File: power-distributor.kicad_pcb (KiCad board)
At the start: 2 copper layers, 99.8 x 18.7 mm, 9 parts, among them J11 Barrel_Jack, J21 Barrel_Jack, J22 Barrel_Jack, J23 Barrel_Jack, J24 Barrel_Jack, J25 Barrel_Jack

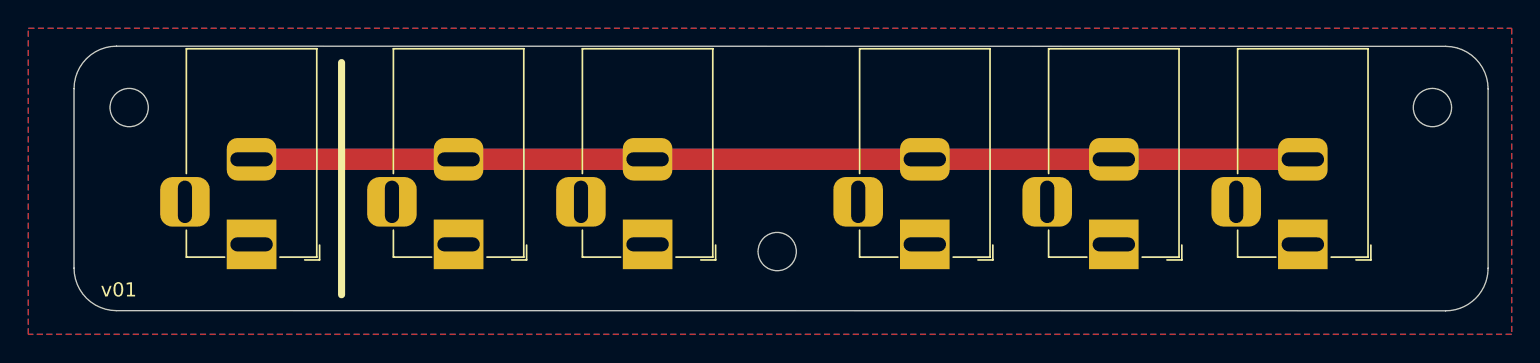
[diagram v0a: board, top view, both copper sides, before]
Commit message: v02: Bigger mounting holes, more even spacing
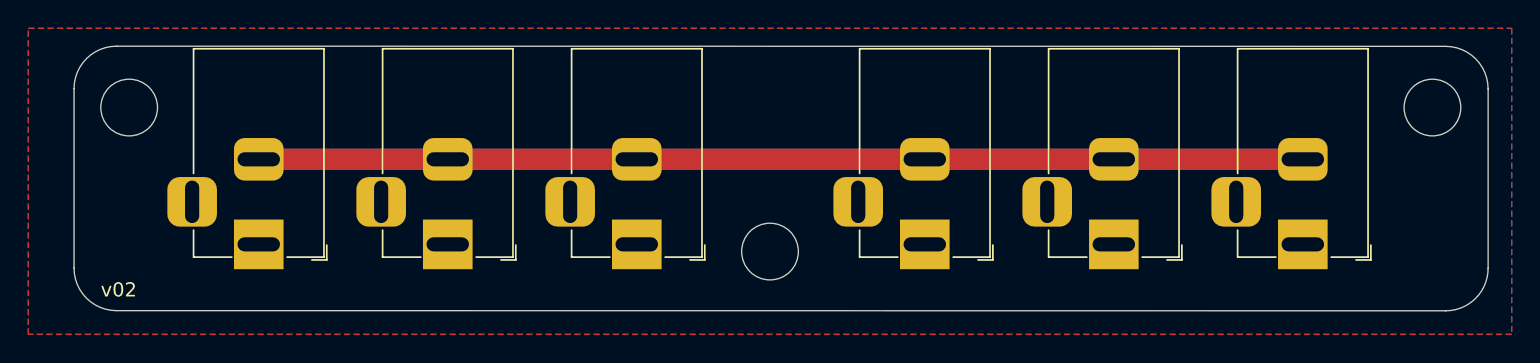
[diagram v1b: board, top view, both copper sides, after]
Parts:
- moved J2 0.76 mm to (92.6, 96.5)
- moved J3 0.76 mm to (105.9, 96.5)
- moved J1 0.51 mm to (79.2, 96.5)
- moved H2 0.51 mm to (115.3, 97.0)
- renumbered J11 to J1, J21 to J2, J22 to J3, J23 to J4, J24 to J5, J25 to J6
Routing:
- net +12V: track 148.0 -> 147.3 mm
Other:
- board text added: "v02"
- board text removed: "v01"
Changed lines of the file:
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@@
 	(net 1 "GND")
 	(net 2 "+12V")
-	(net 3 "unconnected-(J11-Pad3)")
-	(net 4 "unconnected-(J21-Pad3)")
-	(net 5 "unconnected-(J22-Pad3)")
-	(net 6 "unconnected-(J23-Pad3)")
-	(net 7 "unconnected-(J24-Pad3)")
-	(net 8 "unconnected-(J25-Pad3)")
+	(net 3 "unconnected-(J1-Pad3)")
+	(net 4 "unconnected-(J2-Pad3)")
+	(net 5 "unconnected-(J3-Pad3)")
+	(net 6 "unconnected-(J4-Pad3)")
+	(net 7 "unconnected-(J5-Pad3)")
+	(net 8 "unconnected-(J6-Pad3)")
 	(footprint "MountingHole:MountingHole_2.7mm_M2.5"
 		(layer "F.Cu")
@@
 		(pad "" np_thru_hole circle
 			(at 0 0)
-			(size 2.7 2.7)
-			(drill 2.7)
-			(layers "*.Cu" "*.Mask")
+			(size 4 5)
+			(drill 4)
+			(layers "F&B.Cu" "*.Mask")
 		)
 	)
@@
 		(descr "DC Barrel Jack")
 		(tags "Power Jack")
-		(property "Reference" "J23"
+		(property "Reference" "J4"
 			(at -8.45 5.75 90)
 			(layer "F.SilkS")
@@
 			(at -6.2 -5.5 90)
 			(layer "F.Fab")
+			(hide yes)
 			(effects
 				(font
@@
 			(remove_unused_layers no)
 			(roundrect_rratio 0.25)
-			(net 6 "unconnected-(J23-Pad3)")
+			(net 6 "unconnected-(J4-Pad3)")
 			(pintype "passive+no_connect")
 		)
@@
 		(descr "DC Barrel Jack")
 		(tags "Power Jack")
-		(property "Reference" "J24"
+		(property "Reference" "J5"
 			(at -8.45 5.75 90)
 			(layer "F.SilkS")
@@
 			(at -6.2 -5.5 90)
 			(layer "F.Fab")
+			(hide yes)
 			(effects
 				(font
@@
 			(remove_unused_layers no)
 			(roundrect_rratio 0.25)
-			(net 7 "unconnected-(J24-Pad3)")
+			(net 7 "unconnected-(J5-Pad3)")
 			(pintype "passive+no_connect")
 		)
@@
 	(footprint "Connector_BarrelJack:BarrelJack_Horizontal"
 		(layer "F.Cu")
-		(at 78.74 96.52 -90)
+		(at 79.248 96.52 -90)
 		(descr "DC Barrel Jack")
 		(tags "Power Jack")
-		(property "Reference" "J11"
+		(property "Reference" "J1"
 			(at -8.45 5.75 90)
 			(layer "F.SilkS")
@@
 			(at -6.2 -5.5 90)
 			(layer "F.Fab")
+			(hide yes)
 			(effects
 				(font
@@
 			(remove_unused_layers no)
 			(roundrect_rratio 0.25)
-			(net 3 "unconnected-(J11-Pad3)")
+			(net 3 "unconnected-(J1-Pad3)")
 			(pintype "passive+no_connect")
 		)
@@
 		(pad "" np_thru_hole circle
 			(at 0 0)
-			(size 2.7 2.7)
-			(drill 2.7)
-			(layers "*.Cu" "*.Mask")
+			(size 4 5)
+			(drill 4)
+			(layers "F&B.Cu" "*.Mask")
 		)
 	)
 	(footprint "MountingHole:MountingHole_2.7mm_M2.5"
 		(layer "F.Cu")
-		(at 115.824 97.028)
+		(at 115.316 97.028)
 		(descr "Mounting Hole 2.7mm, no annular, M2.5")
 		(tags "mounting hole 2.7mm no annular m2.5")
@@
 		(pad "" np_thru_hole circle
 			(at 0 0)
-			(size 2.7 2.7)
-			(drill 2.7)
-			(layers "*.Cu" "*.Mask")
+			(size 4 5)
+			(drill 4)
+			(layers "F&B.Cu" "*.Mask")
 		)
 	)
@@
 		(descr "DC Barrel Jack")
 		(tags "Power Jack")
-		(property "Reference" "J25"
+		(property "Reference" "J6"
 			(at -8.45 5.75 90)
 			(layer "F.SilkS")
@@
 			(at -6.2 -5.5 90)
 			(layer "F.Fab")
+			(hide yes)
 			(effects
 				(font
@@
 			(remove_unused_layers no)
 			(roundrect_rratio 0.25)
-			(net 8 "unconnected-(J25-Pad3)")
+			(net 8 "unconnected-(J6-Pad3)")
 			(pintype "passive+no_connect")
 		)
@@
 	(footprint "Connector_BarrelJack:BarrelJack_Horizontal"
 		(layer "F.Cu")
-		(at 106.68 96.52 -90)
+		(at 105.918 96.52 -90)
 		(descr "DC Barrel Jack")
 		(tags "Power Jack")
-		(property "Reference" "J22"
+		(property "Reference" "J3"
 			(at -8.45 5.75 90)
 			(layer "F.SilkS")
@@
 			(at -6.2 -5.5 90)
 			(layer "F.Fab")
+			(hide yes)
 			(effects
 				(font
@@
 			(remove_unused_layers no)
 			(roundrect_rratio 0.25)
-			(net 5 "unconnected-(J22-Pad3)")
+			(net 5 "unconnected-(J3-Pad3)")
 			(pintype "passive+no_connect")
 		)
@@
 	(footprint "Connector_BarrelJack:BarrelJack_Horizontal"
 		(layer "F.Cu")
-		(at 93.345 96.52 -90)
+		(at 92.583 96.52 -90)
 		(descr "DC Barrel Jack")
 		(tags "Power Jack")
-		(property "Reference" "J21"
+		(property "Reference" "J2"
 			(at -8.45 5.75 90)
 			(layer "F.SilkS")
@@
 			(at -6.2 -5.5 90)
 			(layer "F.Fab")
+			(hide yes)
 			(effects
 				(font
@@
 			(remove_unused_layers no)
 			(roundrect_rratio 0.25)
-			(net 4 "unconnected-(J21-Pad3)")
+			(net 4 "unconnected-(J2-Pad3)")
 			(pintype "passive+no_connect")
 		)
@@
 			)
 		)
-	)
-	(gr_line
-		(start 85.09 83.693)
-		(end 85.09 100.076)
-		(stroke
-			(width 0.5)
-			(type default)
-		)
-		(layer "F.SilkS")
 	)
 	(gr_line
@@
 		(layer "Edge.Cuts")
 	)
-	(gr_text "v01"
+	(gr_text "v02"
 		(at 68.094 100.3177 0)
 		(layer "F.SilkS")
@@
 	)
 	(segment
-		(start 79.09 90.52)
+		(start 79.248 90.52)
 		(end 152.908 90.52)
 		(width 1.5)
@@
 	)
 	(segment
-		(start 78.74 90.52)
+		(start 79.248 90.52)
 		(end 152.908 90.52)
 		(width 1.5)
